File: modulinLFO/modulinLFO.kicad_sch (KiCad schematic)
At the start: 106 parts, among them J1 Conn_01x06_Pin, Q1 BC548, Q2 BC548, Q3 2N7000, Q4 BC548, Q5 BC548, SW1 SW_SPDT, U1 TL074, U2 LM7805, U3 TL074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

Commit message: Finished up LFO PCB
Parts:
- removed J1: Conn_01x06_Pin, User:TerminalBlock_1x6_CNC, symbol Connector:Conn_01x06_Pin
- removed RV14, RV15, RV17, RV18, RV7: B100k, User:Potentiometer_PanelMount_CNC, symbol Device:R_Potentiometer
- added C10, C11: 100n, User:C_Axial_P5.00mm_CNC, symbol Device:C
- added J1: Screw_Terminal_01x05, User:TerminalBlock_1x5_CNC, symbol Connector:Screw_Terminal_01x05
- added Q6, Q7, Q8: BC548, User:TO-92_CNC, symbol Transistor_BJT:BC548
- added R49: 680k, User:R_10.16mm_CNC, symbol Device:R
- added R50: 680k, User:R_7.62mm_CNC, symbol Device:R
- added R51: 22k, User:R_10.16mm_CNC, symbol Device:R
- added RV14: 100k, User:Potentiometer_Trim_CNC, symbol Device:R_Potentiometer_Trim
- added RV15: 1k, User:Potentiometer_Trim_CNC, symbol Device:R_Potentiometer_Trim
- added SW2: SW_1x4, User:SW_Slide_SP4T_H6.00mm_CNC, symbol Switch:SW_Rotary_1x4_MP
- C22, C23: value 100n -> 100u; footprint User:C_Axial_P5.00mm_CNC -> User:C_Radial_Polarized_P2.5mm_CNC
- R20: value 100k 1% -> 22k; footprint User:R_5.08mm_CNC -> User:R_7.62mm_CNC
- R3: value 100k -> 1k 1%; footprint User:R_2.54mm_CNC -> User:R_7.62mm_CNC
- R31: value 100k 1% -> 100k
- R43: value 220k -> 820
- R44: value 220k -> 22k
- R45: value 220k -> 10k
- R46: value 51k -> 1k 1%; footprint User:R_2.54mm_CNC -> User:R_7.62mm_CNC
- R47: value 22k -> 10k; footprint User:R_2.54mm_CNC -> User:R_10.16mm_CNC
- R48: value 22k -> 10k; footprint User:R_5.08mm_CNC_Alt -> User:R_10.16mm_CNC
- U8: footprint User:DIP8_CNC -> User:DIP-8_CNC
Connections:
- net GND: now also C22.1, C23.2, R43.1, RV16.3, U5.5 (+), C10.2, C11.1, J1.4 (Pin_4), Q6.1 (C), Q8.2 (B), R49.2; no longer C22.2, C23.1, RV16.1, U8.3 (+), U8.5 (+)
- net OUT: now also J1.1 (Pin_1), R50.1
- net PWM: now also SW2.1
- net Sawtooth: now also SW2.2; no longer RV16.3
- net Sine: now also SW2.4
- net Triangle: now also SW2.3
- net VCC: now also C22.2, C10.1, J1.5 (Pin_5), RV14.1, RV15.2; no longer C22.1
- net VEE: now also C23.1, R45.1, C11.2, J1.3 (Pin_3), RV14.3; no longer C23.2
- net at R48.1: now also U8.5 (+), R49.1
- net at R23.2, R24.1, U4.13 (-): no longer R20.2
- net at R44.2: now also Q7.3 (E), Q8.3 (E); no longer RV16.2
- net at R1.2, R2.2, R4.2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: no longer R3.2
- net at R45.2: now also R44.1, Q6.3 (E)
- net at R43.2: now also R42.1, Q7.2 (B)
- net at U5.6 (-), U5.7: no longer R20.1
- net at R42.2: now also SW2.5
- net at R47.1, U8.6 (-): now also R50.2; no longer R48.2
- net LFO renamed EXP
- net EXP: now also RV16.1, J1.2 (Pin_2)
- net NOTE: no longer names the net of R3.1
- net NOTE: now also R47.2, Q7.1 (C)
- new net: R3.2, RV15.1
- new net: Q6.2 (B), R20.1, R51.1
- new net: R20.2, RV14.2
- new net: R51.2, U8.1, U8.2 (-)
- new net: RV16.2, U8.3 (+)
- new net: Q8.1 (C), R46.1, R48.2
- new net: R46.2, RV15.3
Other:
- note added: "Amplitude"
- note added: "Exp Amp Amt"
- note added: "Exp Frq Amt"
- note added: "Shape Select"
- note removed: "Amp"
- note removed: "LFO Frq Amp"
- note removed: "LFO PWM Amp"
- note removed: "Mixing"
- note removed: "PWM Mix"
- note removed: "Saw Mix"
- note removed: "Sine Mix"
- note removed: "Tri Mix"
- moved on the sheet: C19, R31, R4, RV3, U1C

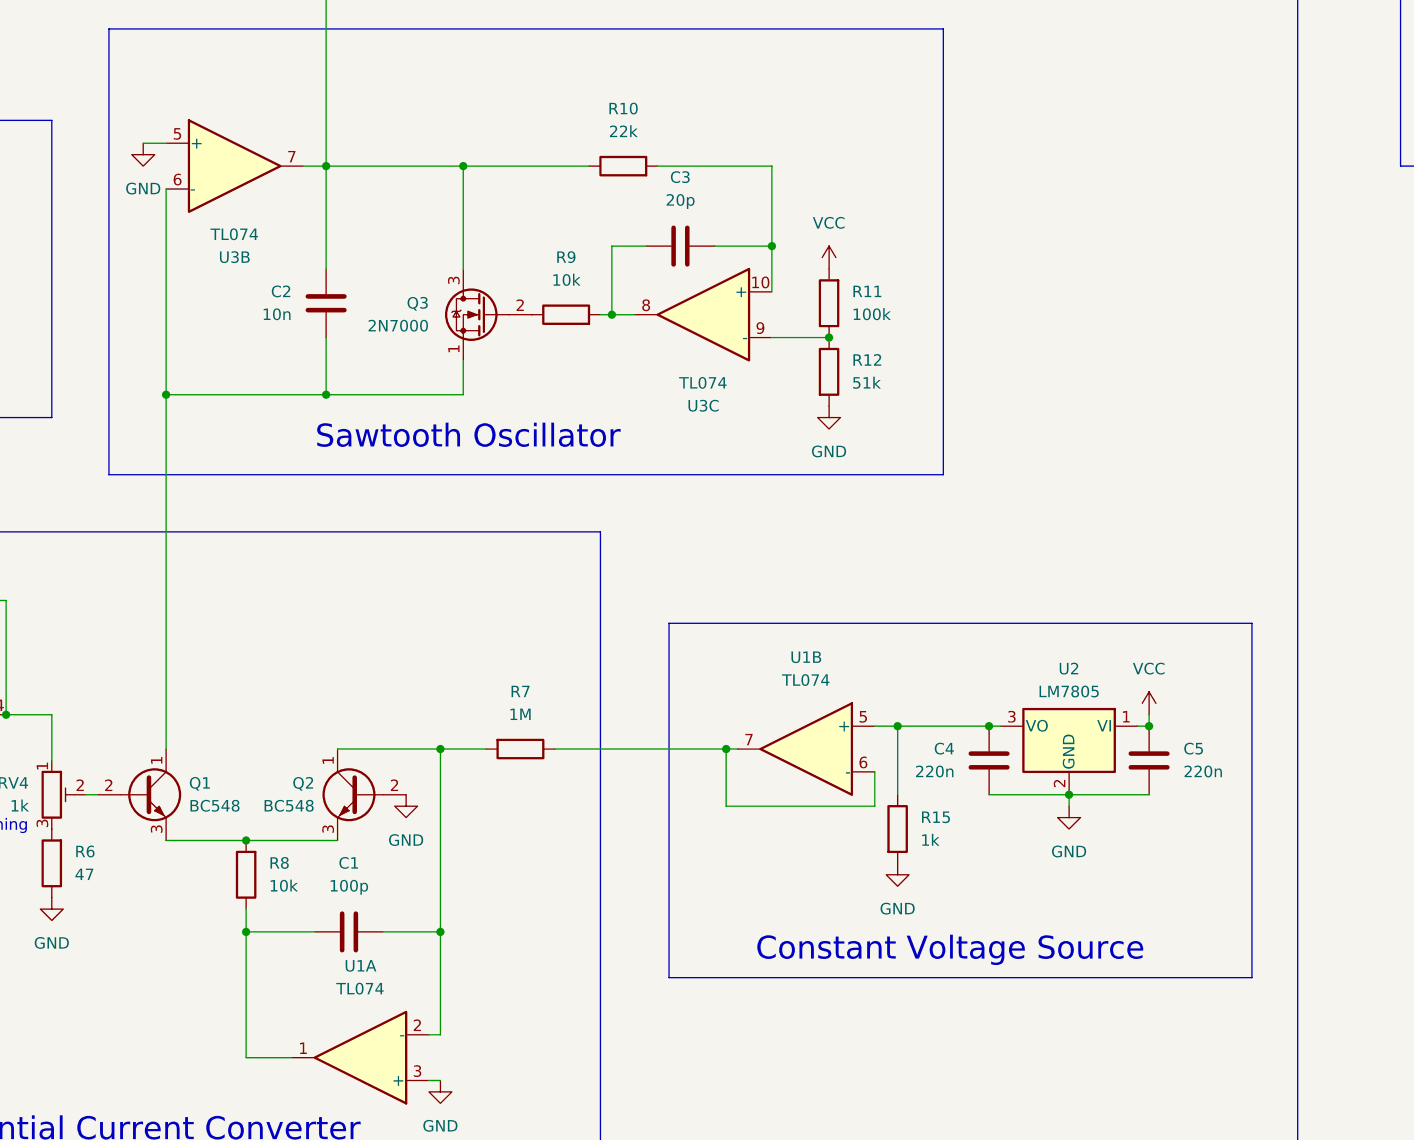
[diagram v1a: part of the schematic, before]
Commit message: Add VCF ciruit and edit for JLCPCB
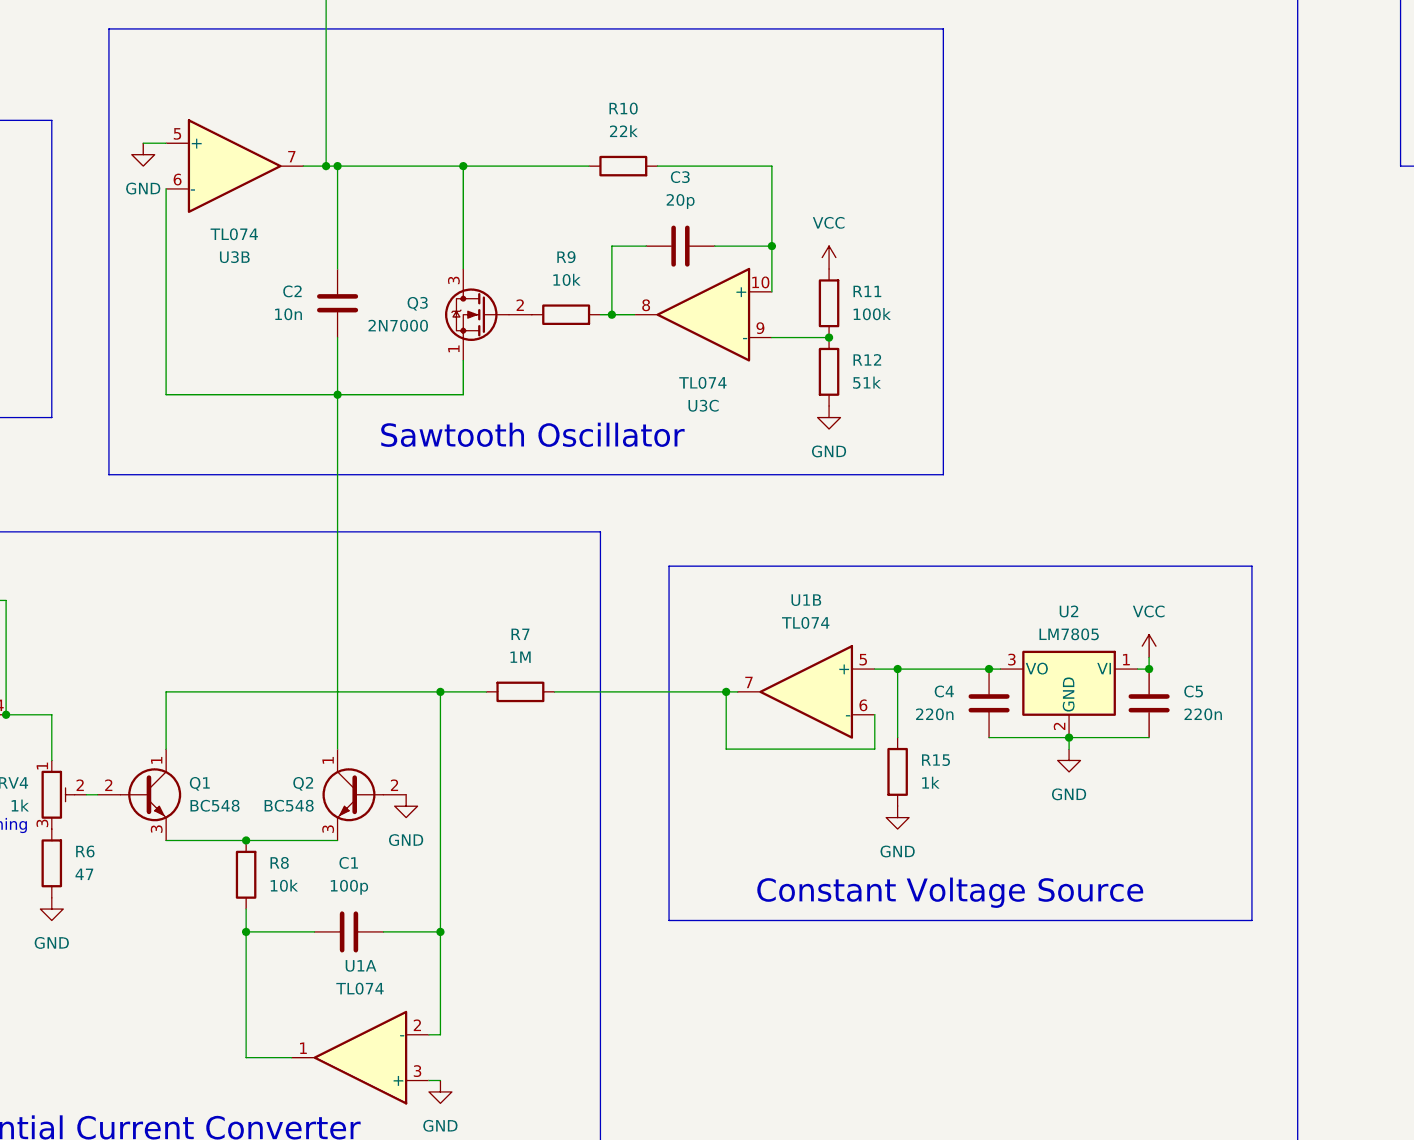
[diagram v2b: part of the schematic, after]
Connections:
- net at C1.2, R7.2, U1.2 (-): now also Q1.1 (C); no longer Q2.1 (C)
- net at C2.2, Q3.1 (S), U3.6 (-): now also Q2.1 (C); no longer Q1.1 (C)
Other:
- moved on the sheet: C2, C4, C5, R15, R7, U1B, U2

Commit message: Add STEP files
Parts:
- SW1: footprint User:SW_Slide_SPST_H6.00mm_CNC -> User:SW_Slide_SPDT_H6.00mm_CNC
- U7: footprint User:DIP8_CNC -> User:DIP-8_CNC
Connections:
- net EXP: now also RV16.3, RV3.3; no longer RV16.1, RV3.1
- net GND: now also RV16.1, RV3.1; no longer RV16.3, RV3.3
- net VCC: now also RV1.3, RV2.3; no longer RV1.1, RV2.1
- net VEE: now also RV1.1, RV2.1; no longer RV1.3, RV2.3
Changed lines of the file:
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@@
 			)
 		)
-		(property "Footprint" "User:DIP8_CNC"
+		(property "Footprint" "User:DIP-8_CNC"
 			(at 321.31 139.7 0)
 			(effects
@@
 		(lib_id "Device:R_Potentiometer")
 		(at 66.04 344.17 0)
+		(mirror x)
 		(unit 1)
 		(exclude_from_sim no)
@@
 		(on_board yes)
 		(dnp no)
-		(fields_autoplaced yes)
 		(property "Reference" "RV1"
-			(at 63.5 342.8999 0)
+			(at 63.5 345.4401 0)
 			(effects
 				(font
@@
 		)
 		(property "Value" "B100k"
-			(at 63.5 345.4399 0)
+			(at 63.5 342.9001 0)
 			(effects
 				(font
@@
 			)
 		)
-		(property "Footprint" "User:DIP8_CNC"
+		(property "Footprint" "User:DIP-8_CNC"
 			(at 120.65 82.55 0)
 			(effects
@@
 		(lib_id "Device:R_Potentiometer")
 		(at 50.8 365.76 0)
+		(mirror x)
 		(unit 1)
 		(exclude_from_sim no)
@@
 		(on_board yes)
 		(dnp no)
-		(fields_autoplaced yes)
 		(property "Reference" "RV3"
-			(at 48.26 364.4899 0)
+			(at 48.26 367.0301 0)
 			(effects
 				(font
@@
 		)
 		(property "Value" "A1M"
-			(at 48.26 367.0299 0)
+			(at 48.26 364.4901 0)
 			(effects
 				(font
@@
 		(lib_id "Device:R_Potentiometer")
 		(at 66.04 322.58 0)
+		(mirror x)
 		(unit 1)
 		(exclude_from_sim no)
@@
 		(on_board yes)
 		(dnp no)
-		(fields_autoplaced yes)
 		(property "Reference" "RV2"
-			(at 63.5 321.3099 0)
+			(at 63.5 323.8501 0)
 			(effects
 				(font
@@
 		)
 		(property "Value" "B100k"
-			(at 63.5 323.8499 0)
+			(at 63.5 321.3101 0)
 			(effects
 				(font
@@
 			)
 		)
-		(property "Footprint" "User:DIP8_CNC"
+		(property "Footprint" "User:DIP-8_CNC"
 			(at 323.85 180.34 0)
 			(effects
@@
 		(lib_id "Device:R_Potentiometer")
 		(at 382.27 171.45 0)
+		(mirror x)
 		(unit 1)
 		(exclude_from_sim no)
@@
 		(on_board yes)
 		(dnp no)
-		(fields_autoplaced yes)
 		(property "Reference" "RV16"
-			(at 379.73 170.1799 0)
+			(at 379.73 172.7201 0)
 			(effects
 				(font
@@
 		)
 		(property "Value" "B100k"
-			(at 379.73 172.7199 0)
+			(at 379.73 170.1801 0)
 			(effects
 				(font
@@
 			)
 		)
-		(property "Footprint" "User:SW_Slide_SPST_H6.00mm_CNC"
+		(property "Footprint" "User:SW_Slide_SPDT_H6.00mm_CNC"
 			(at 154.94 175.26 0)
 			(effects
